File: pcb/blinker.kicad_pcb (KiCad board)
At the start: 2 copper layers, 55.9 x 55.9 mm, 14 parts, among them J1 ISP, U1 ATtiny10-TS

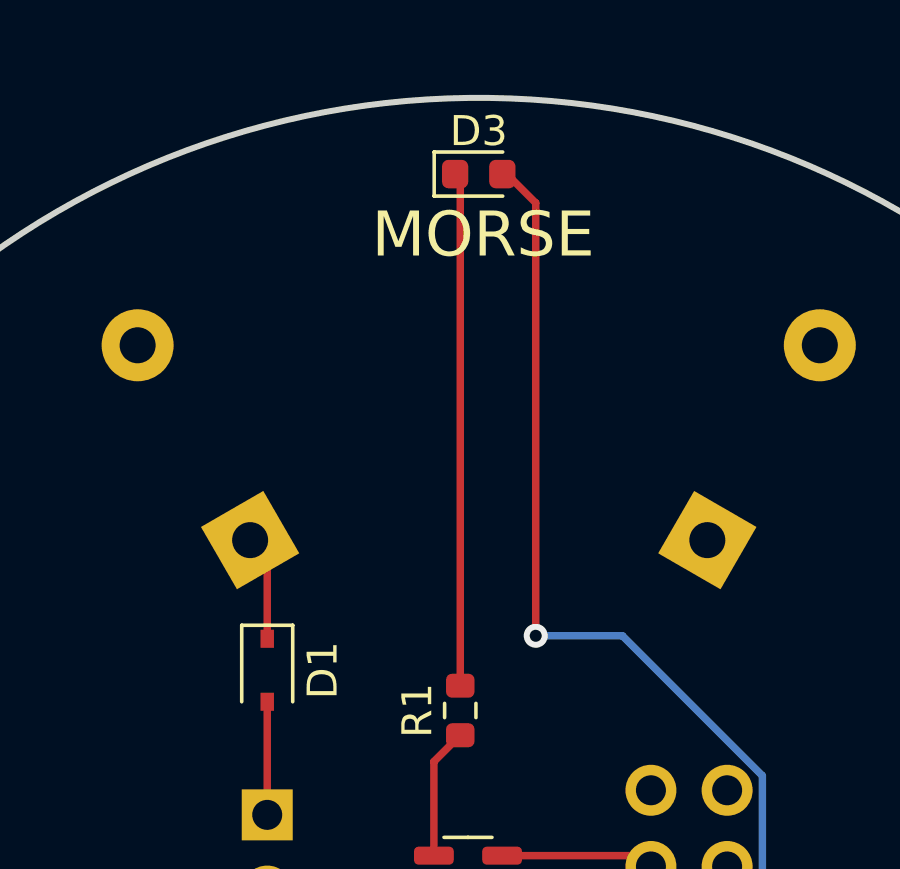
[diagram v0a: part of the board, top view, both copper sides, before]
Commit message: Add through-hole pads for external LED. Reduce thermal relief spoke thickness on fill zones to 0.01 in
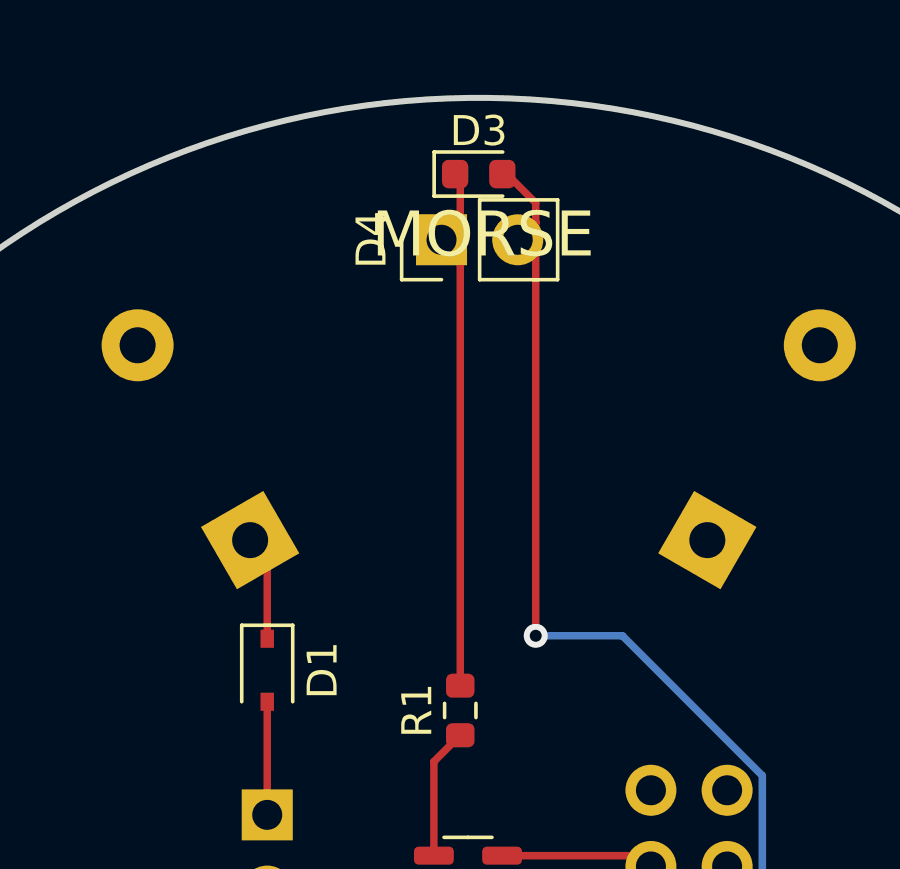
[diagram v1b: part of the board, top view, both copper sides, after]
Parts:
- added D4: LED, Connector_PinHeader_2.54mm:PinHeader_1x02_P2.54mm_Vertical, F.Cu at (163.9, 78.4)
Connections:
- net /LED_R renamed Net-(D3-Pad1)
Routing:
- net 5VCC: track 54.4 -> 55.2 mm
- net Net-(D3-Pad1): track 17.2 -> 17.8 mm
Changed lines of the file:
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@@
   )
   (setup
+    (stackup
+      (layer "F.SilkS" (type "Top Silk Screen"))
+      (layer "F.Paste" (type "Top Solder Paste"))
+      (layer "F.Mask" (type "Top Solder Mask") (thickness 0.01))
+      (layer "F.Cu" (type "copper") (thickness 0.035))
+      (layer "dielectric 1" (type "core") (thickness 1.51) (material "FR4") (epsilon_r 4.5) (loss_tangent 0.02))
+      (layer "B.Cu" (type "copper") (thickness 0.035))
+      (layer "B.Mask" (type "Bottom Solder Mask") (thickness 0.01))
+      (layer "B.Paste" (type "Bottom Solder Paste"))
+      (layer "B.SilkS" (type "Bottom Silk Screen"))
+      (copper_finish "None")
+      (dielectric_constraints no)
+    )
     (pad_to_mask_clearance 0)
     (pcbplotparams
@@
   (net 8 "unconnected-(J1-Pad9)")
   (net 9 "2.7VCC")
-  (net 10 "/LED_R")
+  (net 10 "Net-(D3-Pad1)")
   (net 11 "5VCC")
   (net 12 "LED")
@@
     (fp_line (start 0.8 -0.4) (end -0.5 -0.4) (layer "F.Fab") (width 0.1))
     (pad "1" smd roundrect (at -0.7875 0) (size 0.875 0.95) (layers "F.Cu" "F.Paste" "F.Mask") (roundrect_rratio 0.25)
-      (net 10 "/LED_R") (pinfunction "K") (pintype "passive"))
+      (net 10 "Net-(D3-Pad1)") (pinfunction "K") (pintype "passive"))
     (pad "2" smd roundrect (at 0.7875 0) (size 0.875 0.95) (layers "F.Cu" "F.Paste" "F.Mask") (roundrect_rratio 0.25)
       (net 11 "5VCC") (pinfunction "A") (pintype "passive"))
@@
       (net 12 "LED") (pintype "passive"))
     (pad "2" smd roundrect (at 0.825 0 90) (size 0.8 0.95) (layers "F.Cu" "F.Paste" "F.Mask") (roundrect_rratio 0.25)
-      (net 10 "/LED_R") (pintype "passive"))
+      (net 10 "Net-(D3-Pad1)") (pintype "passive"))
     (model "${KICAD6_3DMODEL_DIR}/Resistor_SMD.3dshapes/R_0603_1608Metric.wrl"
       (offset (xyz 0 0 0))
@@
       (net 5 "RESET") (pinfunction "~{RESET}/PB3") (pintype "bidirectional"))
     (model "${KICAD6_3DMODEL_DIR}/Package_TO_SOT_SMD.3dshapes/SOT-23-6.wrl"
+      (offset (xyz 0 0 0))
+      (scale (xyz 1 1 1))
+      (rotate (xyz 0 0 0))
+    )
+  )
+  (footprint "Connector_PinHeader_2.54mm:PinHeader_1x02_P2.54mm_Vertical" (layer "F.Cu")
+    (at 163.86 78.39 90)
+    (descr "Through hole straight pin header, 1x02, 2.54mm pitch, single row")
+    (tags "Through hole pin header THT 1x02 2.54mm single row")
+    (property "Sheetfile" "blinker.kicad_sch")
+    (property "Sheetname" "")
+    (attr through_hole)
+    (fp_text reference "D4" (at 0 -2.33 90) (layer "F.SilkS")
+      (effects (font (size 1 1) (thickness 0.15)))
+    )
+    (fp_text value "LED" (at 0 4.87 90) (layer "F.Fab")
+      (effects (font (size 1 1) (thickness 0.15)))
+    )
+    (fp_text user "${REFERENCE}" (at 0 1.27) (layer "F.Fab")
+      (effects (font (size 1 1) (thickness 0.15)))
+    )
+    (fp_line (start -1.33 -1.33) (end 0 -1.33) (layer "F.SilkS") (width 0.12))
+    (fp_line (start -1.33 3.87) (end 1.33 3.87) (layer "F.SilkS") (width 0.12))
+    (fp_line (start 1.33 1.27) (end 1.33 3.87) (layer "F.SilkS") (width 0.12))
+    (fp_line (start -1.33 1.27) (end -1.33 3.87) (layer "F.SilkS") (width 0.12))
+    (fp_line (start -1.33 0) (end -1.33 -1.33) (layer "F.SilkS") (width 0.12))
+    (fp_line (start -1.33 1.27) (end 1.33 1.27) (layer "F.SilkS") (width 0.12))
+    (fp_line (start -1.8 -1.8) (end -1.8 4.35) (layer "F.CrtYd") (width 0.05))
+    (fp_line (start 1.8 4.35) (end 1.8 -1.8) (layer "F.CrtYd") (width 0.05))
+    (fp_line (start 1.8 -1.8) (end -1.8 -1.8) (layer "F.CrtYd") (width 0.05))
+    (fp_line (start -1.8 4.35) (end 1.8 4.35) (layer "F.CrtYd") (width 0.05))
+    (fp_line (start -0.635 -1.27) (end 1.27 -1.27) (layer "F.Fab") (width 0.1))
+    (fp_line (start -1.27 -0.635) (end -0.635 -1.27) (layer "F.Fab") (width 0.1))
+    (fp_line (start 1.27 -1.27) (end 1.27 3.81) (layer "F.Fab") (width 0.1))
+    (fp_line (start -1.27 3.81) (end -1.27 -0.635) (layer "F.Fab") (width 0.1))
+    (fp_line (start 1.27 3.81) (end -1.27 3.81) (layer "F.Fab") (width 0.1))
+    (pad "1" thru_hole rect (at 0 0 90) (size 1.7 1.7) (drill 1) (layers *.Cu *.Mask)
+      (net 10 "Net-(D3-Pad1)") (pinfunction "K") (pintype "passive"))
+    (pad "2" thru_hole oval (at 0 2.54 90) (size 1.7 1.7) (drill 1) (layers *.Cu *.Mask)
+      (net 11 "5VCC") (pinfunction "A") (pintype "passive"))
+    (model "${KICAD6_3DMODEL_DIR}/Connector_PinHeader_2.54mm.3dshapes/PinHeader_1x02_P2.54mm_Vertical.wrl"
       (offset (xyz 0 0 0))
       (scale (xyz 1 1 1))
@@
   (segment (start 148.35 105.52) (end 150.65 105.52) (width 0.25) (layer "F.Cu") (net 9))
   (via (at 150.65 105.52) (size 0.8) (drill 0.4) (layers "F.Cu" "B.Cu") (net 9))
-  (segment (start 164.485 93.255) (end 164.485 76.5225) (width 0.25) (layer "F.Cu") (net 10))
+  (segment (start 164.485 78.395) (end 164.485 76.5225) (width 0.25) (layer "F.Cu") (net 10))
+  (segment (start 164.485 93.255) (end 164.485 78.395) (width 0.25) (layer "F.Cu") (net 10))
+  (segment (start 163.86 78.39) (end 164.48 78.39) (width 0.25) (layer "F.Cu") (net 10))
   (segment (start 164.485 76.5225) (end 164.1625 76.2) (width 0.25) (layer "F.Cu") (net 10))
+  (segment (start 164.48 78.39) (end 164.485 78.395) (width 0.25) (layer "F.Cu") (net 10))
   (segment (start 166.6 108.24) (end 172.04 108.24) (width 0.25) (layer "F.Cu") (net 11))
-  (segment (start 167 91.59) (end 167 77.1625) (width 0.25) (layer "F.Cu") (net 11))
+  (segment (start 166.4 78.39) (end 166.98 77.81) (width 0.25) (layer "F.Cu") (net 11))
   (segment (start 163.605 99.87) (end 163.221428 99.87) (width 0.25) (layer "F.Cu") (net 11))
-  (segment (start 167 77.1625) (end 166.0375 76.2) (width 0.25) (layer "F.Cu") (net 11))
+  (segment locked (start 167 77.1625) (end 166.0375 76.2) (width 0.25) (layer "F.Cu") (net 11))
   (segment (start 162.61798 100.473448) (end 162.61798 104.25798) (width 0.25) (layer "F.Cu") (net 11))
+  (segment (start 167 91.59) (end 167 77.81) (width 0.25) (layer "F.Cu") (net 11))
   (segment (start 166.6 108.24) (end 165.75 107.39) (width 0.25) (layer "F.Cu") (net 11))
   (segment (start 162.61798 104.25798) (end 165.75 107.39) (width 0.25) (layer "F.Cu") (net 11))
+  (segment (start 167 77.81) (end 167 77.1625) (width 0.25) (layer "F.Cu") (net 11))
+  (segment (start 166.98 77.81) (end 167 77.81) (width 0.25) (layer "F.Cu") (net 11))
   (segment (start 172.04 108.24) (end 173.38 106.9) (width 0.25) (layer "F.Cu") (net 11))
   (segment (start 163.221428 99.87) (end 162.61798 100.473448) (width 0.25) (layer "F.Cu") (net 11))
@@
     (connect_pads (clearance 0.508))
     (min_thickness 0.254) (filled_areas_thickness no)
-    (fill yes (thermal_gap 0.508) (thermal_bridge_width 0.508))
+    (fill yes (thermal_gap 0.508) (thermal_bridge_width 0.254))
     (polygon
       (pts
@@
     (connect_pads (clearance 0.508))
     (min_thickness 0.254) (filled_areas_thickness no)
-    (fill yes (thermal_gap 0.508) (thermal_bridge_width 0.508))
+    (fill yes (thermal_gap 0.508) (thermal_bridge_width 0.254))
     (polygon
       (pts

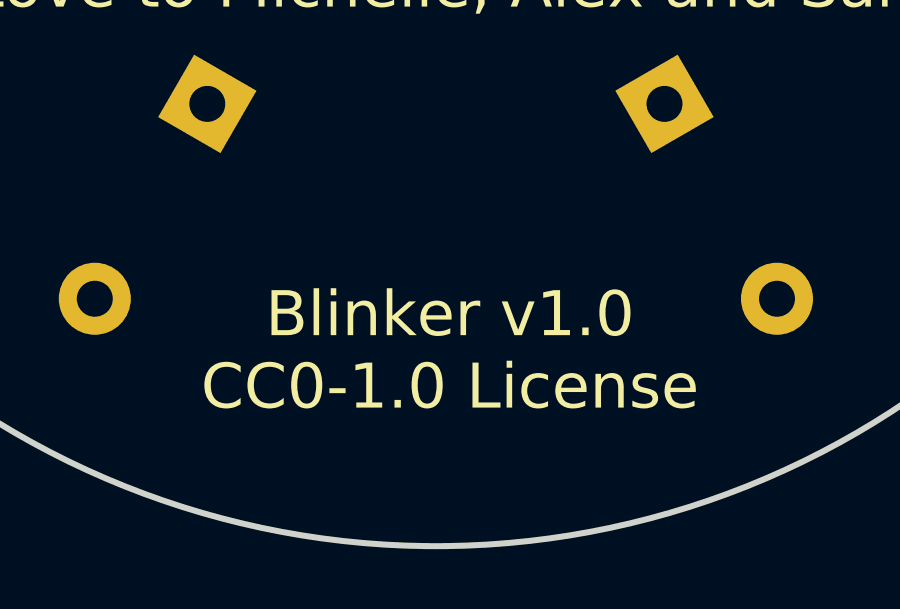
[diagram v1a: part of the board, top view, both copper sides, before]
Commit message: Update version number on silkscreen.
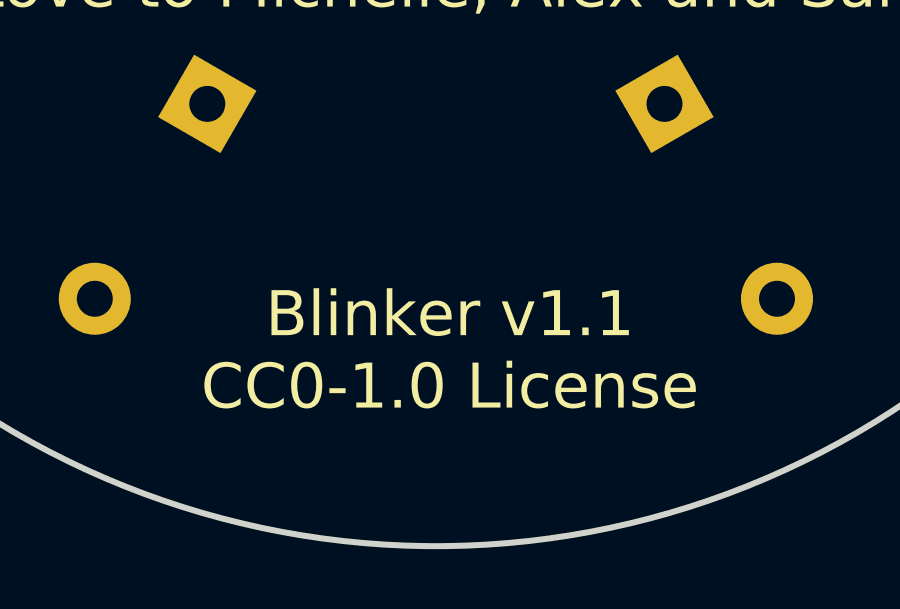
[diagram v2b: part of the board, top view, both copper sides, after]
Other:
- board text added: "Blinker v1.1 CC0-1.0 License"
- board text removed: "Blinker v1.0 CC0-1.0 License"
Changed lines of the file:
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@@
     (effects (font (size 1.5 1.5) (thickness 0.3)) (justify mirror))
   )
-  (gr_text "Blinker v1.0\nCC0-1.0 License " (at 165.57 123.02) (layer "F.SilkS")
+  (gr_text "Blinker v1.1\nCC0-1.0 License " (at 165.57 123.02) (layer "F.SilkS")
     (effects (font (size 1.5 1.5) (thickness 0.3)))
   )

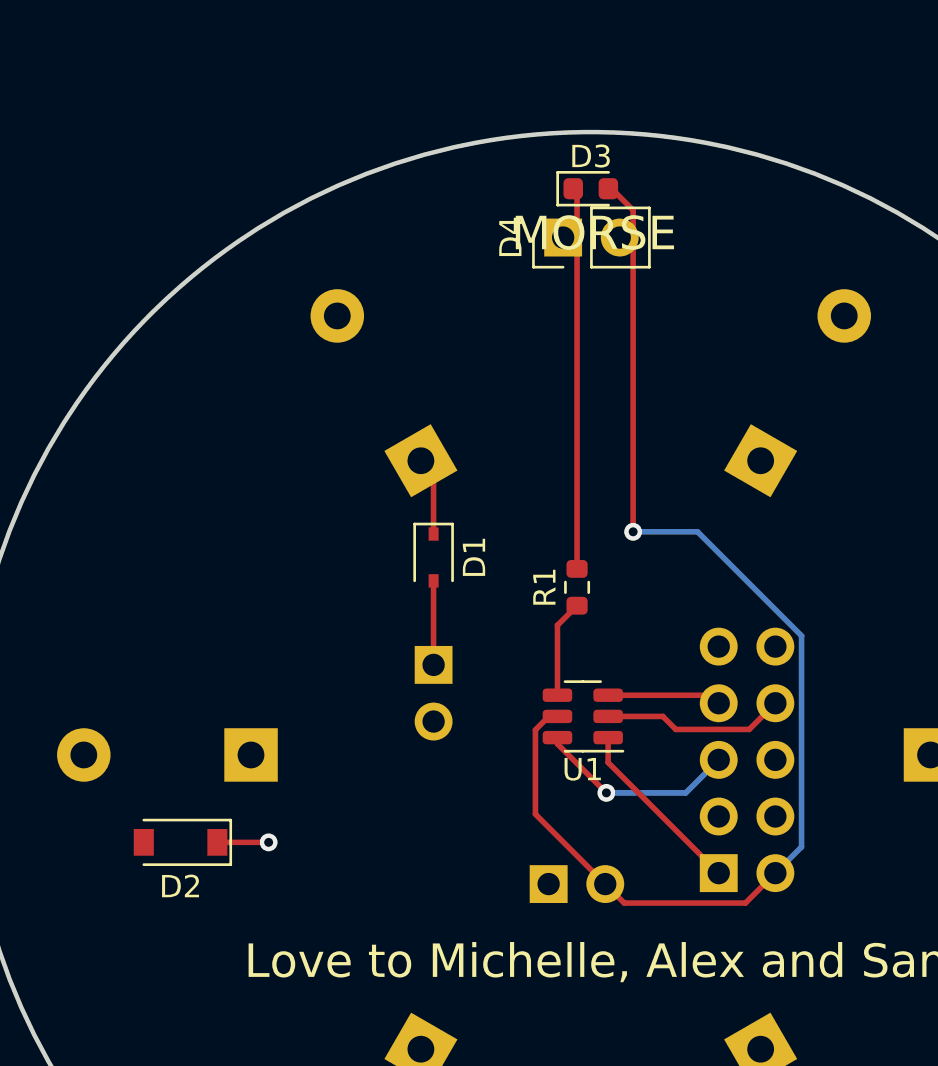
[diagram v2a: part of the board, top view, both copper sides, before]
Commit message: Replace cap disconnect jumper with solder bridge.
Replace 10-pin AVRISP with 6-pad version.

Rearrangements
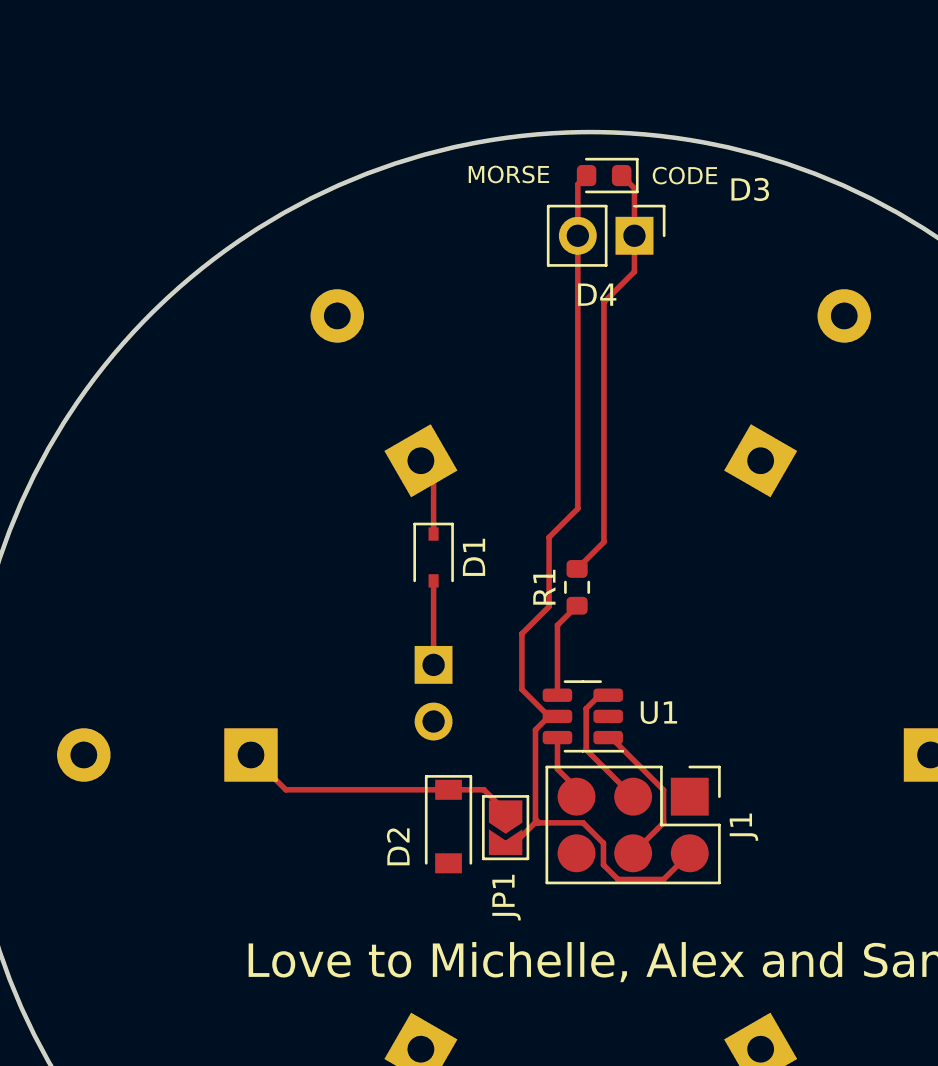
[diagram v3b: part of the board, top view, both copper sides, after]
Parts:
- J1: footprint Connector_PinHeader_2.54mm:PinHeader_2x05_P2.54mm_Vertical -> Blinker:AVRISP_6PAD; moved to F.Cu
- JP1: footprint Connector_PinHeader_2.54mm:PinHeader_1x02_P2.54mm_Vertical -> Jumper:SolderJumper-2_P1.3mm_Open_TrianglePad1.0x1.5mm; moved to F.Cu
- moved D2 12.0 mm to (158.7, 104.8), turned to -90 degrees
- moved J1 3.67 mm to (169.5, 103.5), turned to -90 degrees
- moved D4 3.20 mm to (167.1, 78.3), turned to -90 degrees
- moved JP1 3.18 mm to (161.3, 104.9)
- moved D3 0.84 mm to (165.7, 75.6), turned to 180 degrees
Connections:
- J1 pad 1: TPIDATA -> unconnected-(J1-Pad1)
- J1 pad 3: GND -> TPICLK
- J1 pad 4: unconnected-(J1-Pad4) -> TPIDATA
- J1 pad 6: unconnected-(J1-Pad6) -> GND
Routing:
- net 5VCC: track 55.2 -> 42.1 mm, vias 1 -> 0
- net 2.7VCC: track 5.82 -> 16.0 mm, vias 1 -> 0
- net GND: track 8.23 -> 0.00 mm
- net RESET: track 9.04 -> 2.62 mm, vias 1 -> 0
- net TPIDATA: track 8.13 -> 6.73 mm
- net Net-(D3-Pad1): track 17.8 -> 18.9 mm
- net TPICLK: track 5.11 -> 5.67 mm
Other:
- board text added: "+ -"
- board text added: "CODE"
